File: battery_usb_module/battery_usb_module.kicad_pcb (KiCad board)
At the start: 2 copper layers, 6 parts, among them J1 USB_C_Receptacle_USB2.0_16P, J2 DF12NC_3.0_-60DS-0.5V_51_, J3 Conn_01x02_MountingPin, U1 LP3947

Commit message: PCB Edge cuts and layout
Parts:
- moved J1 33.1 mm to (138.5, 100.5)
- moved U1 16.3 mm to (188.1, 110.0)
- moved C1 16.0 mm to (188.0, 115.0)
- moved C2 15.0 mm to (192.0, 111.0)
- moved J2 12.6 mm to (173.2, 114.3)
- moved J3 6.12 mm to (192.0, 115.0)
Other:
- board outline added: 58.5 x 30.5 mm
- board text added: "Stiffener"
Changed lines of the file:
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@@
 	(footprint "Package_SON:WSON-14-1EP_4.0x4.0mm_P0.5mm_EP2.6x2.6mm"
 		(layer "F.Cu")
-		(at 171.85 109.425)
+		(at 188.1 110)
 		(descr "14-Lead Plastic Dual Flat, No Lead Package - 4.0x4.0x0.8 mm Body [WSON], http://www.ti.com/lit/ml/mpds421/mpds421.pdf")
 		(tags "NHL014B")
@@
 			(at 0 4.7 270)
 			(layer "F.Fab")
+			(hide yes)
 			(effects
 				(font
@@
 	(footprint "Capacitor_SMD:C_0603_1608Metric"
 		(layer "F.Cu")
-		(at 172 114.275 -90)
+		(at 188 115 -90)
 		(descr "Capacitor SMD 0603 (1608 Metric), square (rectangular) end terminal, IPC-7351 nominal, (Body size source: IPC-SM-782 page 76, https://www.pcb-3d.com/wordpress/wp-content/uploads/ipc-sm-782a_amendment_1_and_2.pdf), generated with kicad-footprint-generator")
 		(tags "capacitor")
 		(property "Reference" "C1"
-			(at 0 -1.43 90)
+			(at -2 0 180)
 			(layer "F.SilkS")
 			(effects
@@
 	(footprint "Connector_Hirose:Hirose_DF12_DF12E3.0-60DP-0.5V_2x30_P0.50mm_Vertical"
 		(layer "F.Cu")
-		(at 178.75 102.975)
+		(at 173.25 114.3)
 		(descr "Hirose DF12E SMD, DF12E3.0-60DP-0.5V, 60 Pins per row (https://www.hirose.com/product/document?clcode=CL0537-0834-6-81&productname=DF12E(3.0)-50DP-0.5V(81)&series=DF12&documenttype=2DDrawing&lang=en&documentid=0000992393), generated with kicad-footprint-generator")
 		(tags "connector Hirose DF12 vertical")
@@
 			(at 0 4.1 0)
 			(layer "F.Fab")
+			(hide yes)
 			(effects
 				(font
@@
 	(footprint "Capacitor_SMD:C_0603_1608Metric"
 		(layer "F.Cu")
-		(at 177 110.775 90)
+		(at 192 111 90)
 		(descr "Capacitor SMD 0603 (1608 Metric), square (rectangular) end terminal, IPC-7351 nominal, (Body size source: IPC-SM-782 page 76, https://www.pcb-3d.com/wordpress/wp-content/uploads/ipc-sm-782a_amendment_1_and_2.pdf), generated with kicad-footprint-generator")
 		(tags "capacitor")
 		(property "Reference" "C2"
-			(at 0.42 -6.5 0)
+			(at 2 0 0)
 			(layer "F.SilkS")
 			(effects
@@
 		)
 		(property "Value" "1uF"
-			(at 0 1.43 90)
+			(at 0 1.5 90)
 			(layer "F.Fab")
 			(effects
@@
 	(footprint "Connector_PinHeader_1.00mm:PinHeader_1x02_P1.00mm_Vertical_SMD_Pin1Left"
 		(layer "F.Cu")
-		(at 186 113.775 90)
+		(at 192 115 90)
 		(descr "surface-mounted straight pin header, 1x02, 1.00mm pitch, single row, style 1 (pin 1 left)")
 		(tags "Surface mounted pin header SMD 1x02 1.00mm single row style1 pin1 left")
@@
 			(at 0 2.11 90)
 			(layer "F.Fab")
+			(hide yes)
 			(effects
 				(font
@@
 	(footprint "Connector_USB:USB_C_Receptacle_GCT_USB4105-xx-A_16P_TopMnt_Horizontal"
 		(layer "F.Cu")
-		(at 116.5 75.775 -90)
+		(at 138.5 100.5 -90)
 		(descr "USB 2.0 Type C Receptacle, GCT, 16P, top mounted, horizontal, 5A: https://gct.co/files/drawings/usb4105.pdf")
 		(tags "USB C Type-C Receptacle SMD USB 2.0 16P 16C USB4105-15-A USB4105-15-A-060 USB4105-15-A-120 USB4105-GF-A USB4105-GF-A-060 USB4105-GF-A-120")
@@
 			)
 		)
+	)
+	(gr_rect
+		(start 161 106)
+		(end 194.5 117.5)
+		(stroke
+			(width 0.3)
+			(type solid)
+		)
+		(fill no)
+		(layer "Dwgs.User")
+	)
+	(gr_line
+		(start 148 106)
+		(end 190.5 106)
+		(stroke
+			(width 0.05)
+			(type default)
+		)
+		(layer "Edge.Cuts")
+	)
+	(gr_arc
+		(start 140 117.5)
+		(mid 137.171573 116.328427)
+		(end 136 113.5)
+		(stroke
+			(width 0.05)
+			(type default)
+		)
+		(layer "Edge.Cuts")
+	)
+	(gr_line
+		(start 194.5 110)
+		(end 194.5 113.5)
+		(stroke
+			(width 0.05)
+			(type default)
+		)
+		(layer "Edge.Cuts")
+	)
+	(gr_line
+		(start 190.5 117.5)
+		(end 140 117.5)
+		(stroke
+			(width 0.05)
+			(type default)
+		)
+		(layer "Edge.Cuts")
+	)
+	(gr_line
+		(start 136 87)
+		(end 146 87)
+		(stroke
+			(width 0.05)
+			(type default)
+		)
+		(layer "Edge.Cuts")
+	)
+	(gr_arc
+		(start 194.5 113.5)
+		(mid 193.328427 116.328427)
+		(end 190.5 117.5)
+		(stroke
+			(width 0.05)
+			(type default)
+		)
+		(layer "Edge.Cuts")
+	)
+	(gr_line
+		(start 136 111)
+		(end 136 87)
+		(stroke
+			(width 0.05)
+			(type default)
+		)
+		(layer "Edge.Cuts")
+	)
+	(gr_arc
+		(start 148 106)
+		(mid 146.585786 105.414214)
+		(end 146 104)
+		(stroke
+			(width 0.05)
+			(type default)
+		)
+		(layer "Edge.Cuts")
+	)
+	(gr_line
+		(start 136 113.5)
+		(end 136 110)
+		(stroke
+			(width 0.05)
+			(type default)
+		)
+		(layer "Edge.Cuts")
+	)
+	(gr_arc
+		(start 190.5 106)
+		(mid 193.328427 107.171573)
+		(end 194.5 110)
+		(stroke
+			(width 0.05)
+			(type default)
+		)
+		(layer "Edge.Cuts")
+	)
+	(gr_line
+		(start 146 87)
+		(end 146 104)
+		(stroke
+			(width 0.05)
+			(type solid)
+		)
+		(layer "Edge.Cuts")
+	)
+	(gr_text "Stiffener"
+		(at 196.5 104.5 0)
+		(layer "Dwgs.User")
+		(effects
+			(font
+				(size 5 5)
+				(thickness 1)
+				(bold yes)
+			)
+			(justify left bottom)
+		)
+	)
+	(dimension
+		(type orthogonal)
+		(layer "Dwgs.User")
+		(pts
+			(xy 190.5 106) (xy 190.5 117.5)
+		)
+		(height 16.5)
+		(orientation 1)
+		(format
+			(prefix "")
+			(suffix "")
+			(units 3)
+			(units_format 0)
+			(precision 4)
+			(suppress_zeroes yes)
+		)
+		(style
+			(thickness 0.1)
+			(arrow_length 1.27)
+			(text_position_mode 0)
+			(arrow_direction outward)
+			(extension_height 0.58642)
+			(extension_offset 0.5)
+			(keep_text_aligned yes)
+		)
+		(gr_text "11.5"
+			(at 205.85 111.75 90)
+			(layer "Dwgs.User")
+			(effects
+				(font
+					(size 1 1)
+					(thickness 0.15)
+				)
+			)
+		)
+	)
+	(dimension
+		(type orthogonal)
+		(layer "Dwgs.User")
+		(pts
+			(xy 194.5 111.75) (xy 136 111.75)
+		)
+		(height -33.75)
+		(orientation 0)
+		(format
+			(prefix "")
+			(suffix "")
+			(units 3)
+			(units_format 0)
+			(precision 4)
+			(suppress_zeroes yes)
+		)
+		(style
+			(thickness 0.1)
+			(arrow_length 1.27)
+			(text_position_mode 0)
+			(arrow_direction outward)
+			(extension_height 0.58642)
+			(extension_offset 0.5)
+			(keep_text_aligned yes)
+		)
+		(gr_text "58.5"
+			(at 165.25 76.85 0)
+			(layer "Dwgs.User")
+			(effects
+				(font
+					(size 1 1)
+					(thickness 0.15)
+				)
+			)
+		)

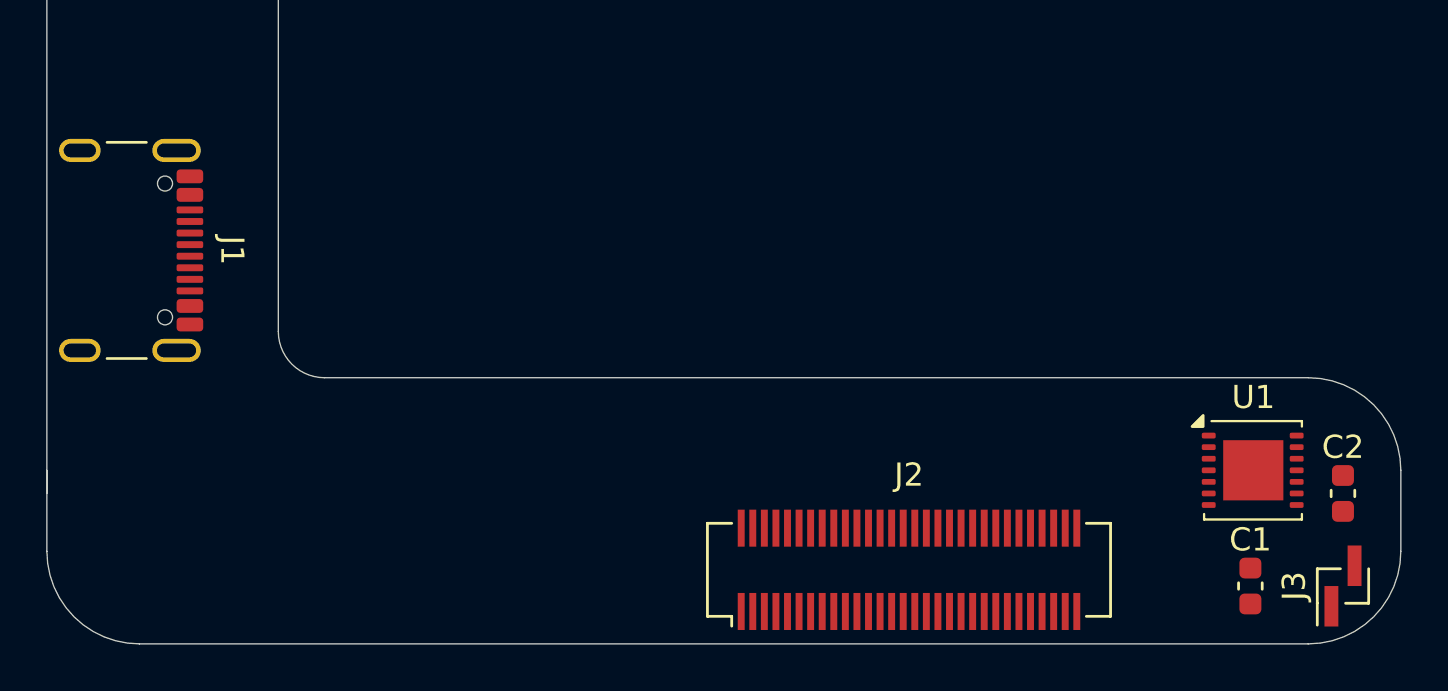
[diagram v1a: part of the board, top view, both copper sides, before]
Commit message: Routed battery module pcb
Completed routing for the battery module section of the modular phone PCB.
This update connects the battery modules to the main power bus and control lines,
ensuring proper power distribution and modular interchangeability.
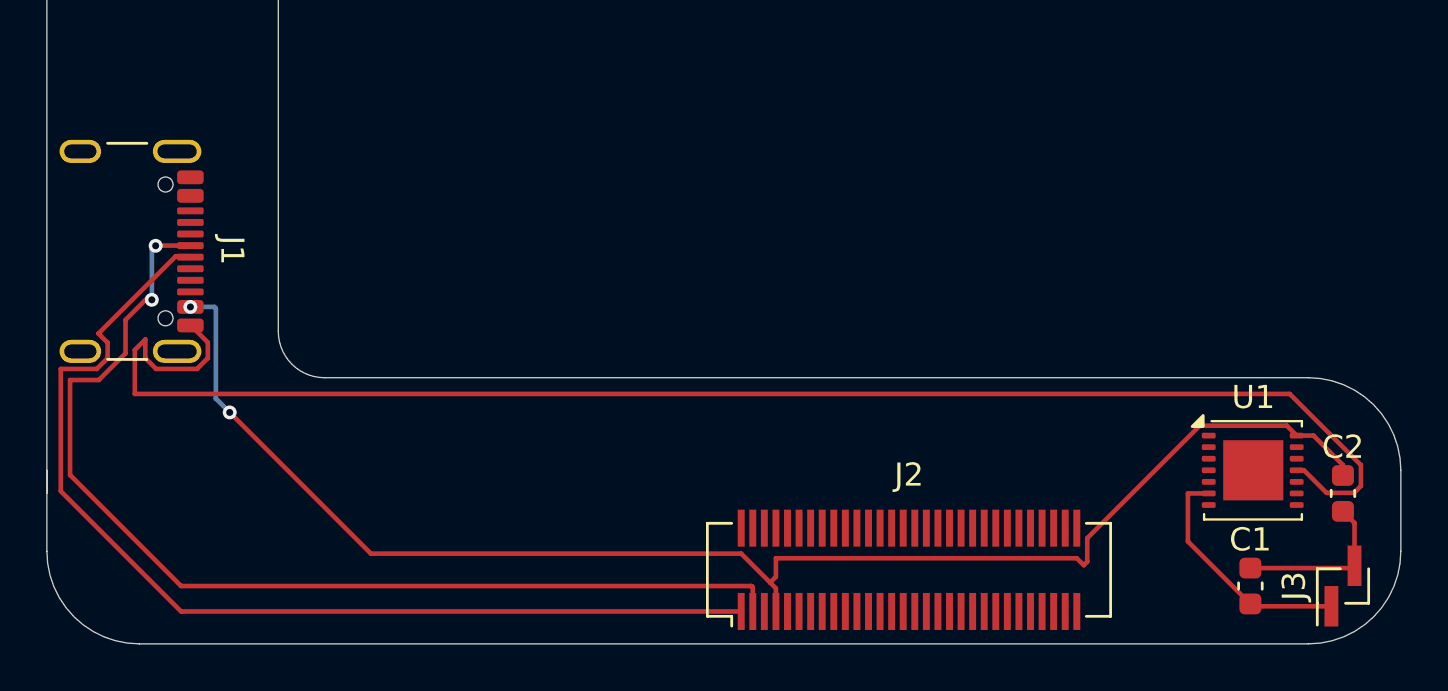
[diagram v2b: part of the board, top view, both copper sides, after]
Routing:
- net Net-(U1-GND): track 0.00 -> 66.7 mm
- net Net-(U1-CHG_IN): track 0.00 -> 63.6 mm, vias 0 -> 2
- net Net-(J1-D+-PadA6): track 0.00 -> 46.5 mm, vias 0 -> 2
- net Net-(J1-D--PadA7): track 0.00 -> 45.6 mm
- net Net-(J3-Pin_1): track 0.00 -> 10.3 mm
- net GND: track 0.00 -> 7.10 mm

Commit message: Removed uneccesary stiffiner labels on user drawings
Stiffiner labels not necesarry since the idea of the battery module being a flex pcb got scrapped
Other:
- board text removed: "Stiffener"
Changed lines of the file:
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@@
 		)
-	)
-	(gr_rect
-		(start 161 106)
-		(end 194.5 117.5)
-		(stroke
-			(width 0.3)
-			(type solid)
-		)
-		(fill no)
-		(layer "Dwgs.User")
 	)
 	(gr_line
@@
 		(layer "Edge.Cuts")
 	)
-	(gr_text "Stiffener"
-		(at 196.5 104.5 0)
-		(layer "Dwgs.User")
-		(effects
-			(font
-				(size 5 5)
-				(thickness 1)
-				(bold yes)
-			)
-			(justify left bottom)
-		)
-	)
 	(dimension

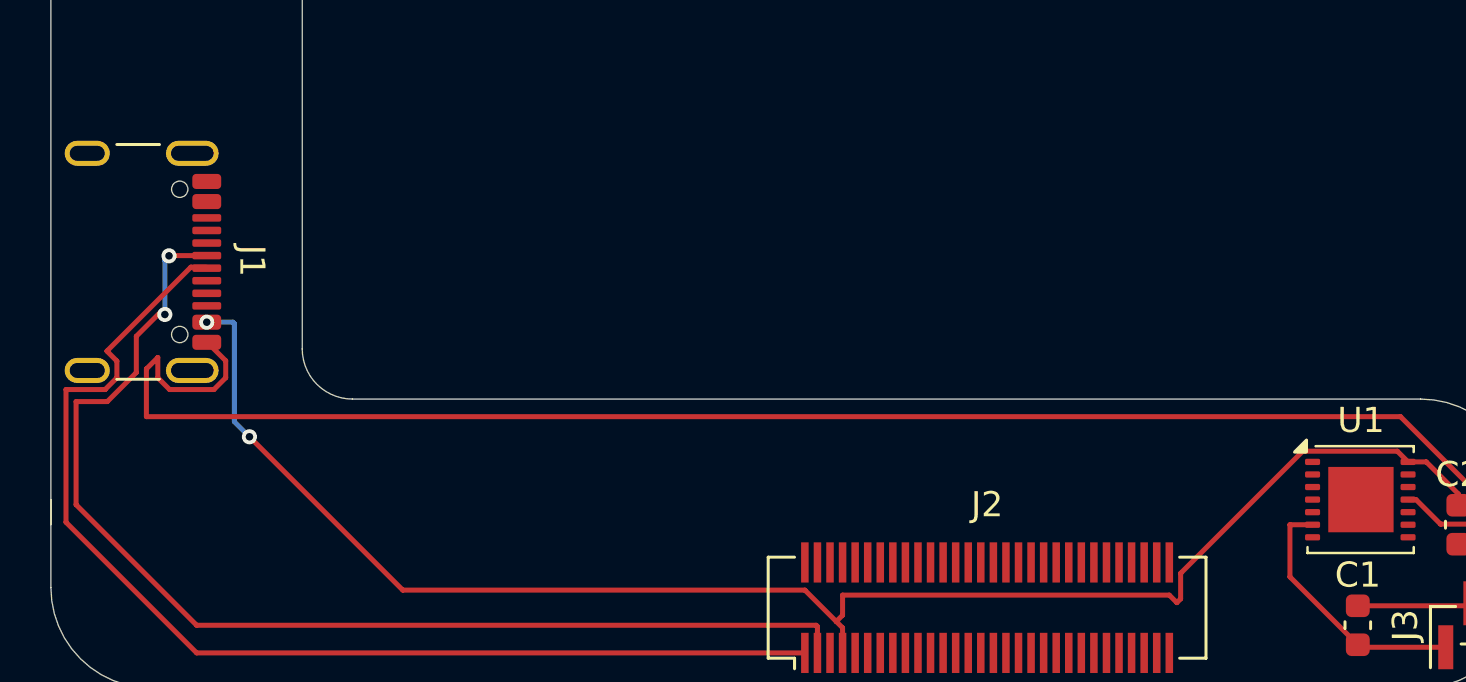
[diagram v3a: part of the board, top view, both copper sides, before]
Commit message: Fixed some wrong routing and added missed routing
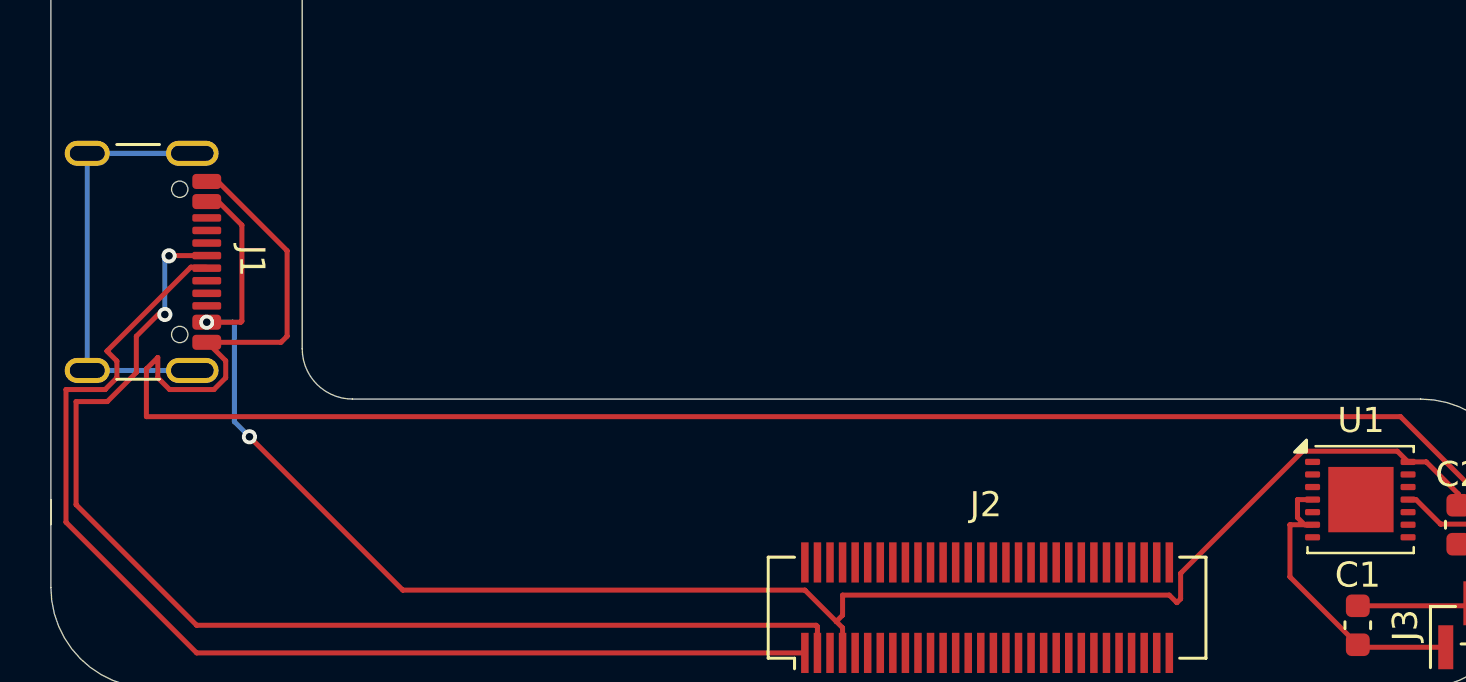
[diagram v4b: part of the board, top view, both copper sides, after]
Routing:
- net unconnected-(J1-SHIELD-PadS1): track 0.00 -> 17.0 mm
- net Net-(U1-GND): track 66.7 -> 77.7 mm
- net Net-(U1-CHG_IN): track 63.6 -> 70.7 mm
- net Net-(J3-Pin_1): track 10.3 -> 12.4 mm
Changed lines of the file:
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@@
 		(tags "connector Hirose DF12 vertical")
 		(property "Reference" "J2"
-			(at 0 -4.1 0)
+			(at -0.05 -4.1 0)
 			(layer "F.SilkS")
 			(effects
@@
 		(layer "Dwgs.User")
 		(pts
-			(xy 194.5 111.75) (xy 136 111.75)
+			(xy 194.45 111.75) (xy 135.95 111.75)
 		)
 		(height -33.75)
@@
 		)
 		(gr_text "58.5"
-			(at 165.25 76.85 0)
+			(at 165.2 76.85 0)
 			(layer "Dwgs.User")
 			(effects
@@
 			)
 		)
+	)
+	(segment
+		(start 142.201492 97.341514)
+		(end 142.641514 97.341514)
+		(width 0.2)
+		(layer "F.Cu")
+		(net 1)
 	)
 	(segment
@@
 	)
 	(segment
+		(start 145.399 100.099)
+		(end 145.399 103.499)
+		(width 0.2)
+		(layer "F.Cu")
+		(net 1)
+	)
+	(segment
 		(start 142.956 105.151785)
 		(end 142.956 104.476)
@@
 	)
 	(segment
+		(start 145.399 103.499)
+		(end 145.156486 103.741514)
+		(width 0.2)
+		(layer "F.Cu")
+		(net 1)
+	)
+	(segment
+		(start 142.641514 97.341514)
+		(end 145.399 100.099)
+		(width 0.2)
+		(layer "F.Cu")
+		(net 1)
+	)
+	(segment
 		(start 139.8 106.7)
 		(end 139.8 104.8)
@@
 	)
 	(segment
+		(start 145.156486 103.741514)
+		(end 142.201492 103.741514)
+		(width 0.2)
+		(layer "F.Cu")
+		(net 1)
+	)
+	(segment
 		(start 142.956 104.476)
 		(end 142.18 103.7)
@@
 	)
 	(segment
+		(start 185.6 110.715798)
+		(end 185.6 110)
+		(width 0.2)
+		(layer "F.Cu")
+		(net 2)
+	)
+	(segment
+		(start 185.6 110)
+		(end 186.2 110)
+		(width 0.2)
+		(layer "F.Cu")
+		(net 2)
+	)
+	(segment
+		(start 185.884202 111)
+		(end 185.6 110.715798)
+		(width 0.2)
+		(layer "F.Cu")
+		(net 2)
+	)
+	(segment
 		(start 185.3 111)
 		(end 186.2 111)
@@
 	)
 	(segment
+		(start 186.2 111)
+		(end 185.884202 111)
+		(width 0.2)
+		(layer "F.Cu")
+		(net 2)
+	)
+	(segment
 		(start 188.1 115.875)
 		(end 188 115.775)
@@
 	)
 	(segment
+		(start 142.660316 98.141514)
+		(end 143.6 99.081198)
+		(width 0.2)
+		(layer "F.Cu")
+		(net 13)
+	)
+	(segment
 		(start 167.5 113.8)
 		(end 167.5 114.6)
@@
 	)
 	(segment
+		(start 142.201492 98.141514)
+		(end 142.660316 98.141514)
+		(width 0.2)
+		(layer "F.Cu")
+		(net 13)
+	)
+	(segment
 		(start 192 109.775)
 		(end 192 110.225)
@@
 	)
 	(segment
+		(start 143.6 99.081198)
+		(end 143.6 102.9)
+		(width 0.2)
+		(layer "F.Cu")
+		(net 13)
+	)
+	(segment
 		(start 180.5 113.8)
 		(end 167.5 113.8)
@@
 	)
 	(segment
+		(start 143.6 102.9)
+		(end 143.558486 102.941514)
+		(width 0.2)
+		(layer "F.Cu")
+		(net 13)
+	)
+	(segment
 		(start 190.725 108.5)
 		(end 192 109.775)
@@
 		(start 180.951 113.949)
 		(end 180.8 114.1)
+		(width 0.2)
+		(layer "F.Cu")
+		(net 13)
+	)
+	(segment
+		(start 143.558486 102.941514)
+		(end 142.201492 102.941514)
 		(width 0.2)
 		(layer "F.Cu")
@@
 	)
 	(segment
+		(start 141.626492 96.221514)
+		(end 137.446492 96.221514)
+		(width 0.2)
+		(layer "B.Cu")
+		(net 16)
+	)
+	(segment
+		(start 137.446492 104.861514)
+		(end 137.446492 96.221514)
+		(width 0.2)
+		(layer "B.Cu")
+		(net 16)
+	)
+	(segment
+		(start 137.446492 104.861514)
+		(end 141.626492 104.861514)
+		(width 0.2)
+		(layer "B.Cu")
+		(net 16)
+	)
+	(segment
